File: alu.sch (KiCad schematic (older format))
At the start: 10 parts

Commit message: tiny fixes in annotation
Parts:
- U20: renamed from U?; footprint (none) -> Package_SO:TSSOP-14_4.4x5mm_P0.65mm; LCSC (none) -> C6807
- gave numbers to parts that had none: 3
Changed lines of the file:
@@
 AR Path="/5FEB4D4D/601578DD" Ref="U?"  Part="1"
 AR Path="/600A4AF3/600A5215/601578DD" Ref="U?"  Part="4"
-AR Path="/600A4AF3/601578DD" Ref="U?"  Part="1"
-F 0 "U?" H 8325 4975 50  0000 C CNN
+AR Path="/600A4AF3/601578DD" Ref="U21"  Part="1"
+F 0 "U21" H 8325 4975 50  0000 C CNN
 F 1 "74HC32" H 8325 4884 50  0000 C CNN
 F 2 "Housings_SOIC:SOIC-14_3.9x8.7mm_Pitch1.27mm" H 7800 4900 50  0001 C CNN
@@
 AR Path="/5FEB4D4D/60158F2A" Ref="U?"  Part="1"
 AR Path="/600A4AF3/600A5215/60158F2A" Ref="U?"  Part="4"
-AR Path="/600A4AF3/60158F2A" Ref="U?"  Part="3"
-F 0 "U?" H 8825 5225 50  0000 C CNN
+AR Path="/600A4AF3/60158F2A" Ref="U21"  Part="3"
+F 0 "U21" H 8825 5225 50  0000 C CNN
 F 1 "74HC32" H 8825 5134 50  0000 C CNN
 F 2 "Housings_SOIC:SOIC-14_3.9x8.7mm_Pitch1.27mm" H 8300 5150 50  0001 C CNN
@@
 AR Path="/5FEB4D4D/60159879" Ref="U?"  Part="1"
 AR Path="/600A4AF3/600A5215/60159879" Ref="U?"  Part="4"
-AR Path="/600A4AF3/60159879" Ref="U?"  Part="2"
-F 0 "U?" H 8325 5475 50  0000 C CNN
+AR Path="/600A4AF3/60159879" Ref="U21"  Part="2"
+F 0 "U21" H 8325 5475 50  0000 C CNN
 F 1 "74HC32" H 8325 5384 50  0000 C CNN
 F 2 "Housings_SOIC:SOIC-14_3.9x8.7mm_Pitch1.27mm" H 7800 5400 50  0001 C CNN
@@
 AR Path="/5FEB4D4D/601666B3" Ref="U?"  Part="1"
 AR Path="/600A4AF3/600A5215/601666B3" Ref="U?"  Part="4"
-AR Path="/600A4AF3/601666B3" Ref="U?"  Part="5"
-F 0 "U?" H 5725 7425 50  0000 C CNN
+AR Path="/600A4AF3/601666B3" Ref="U21"  Part="5"
+F 0 "U21" H 5725 7425 50  0000 C CNN
 F 1 "74HC32" H 5725 7334 50  0000 C CNN
 F 2 "Housings_SOIC:SOIC-14_3.9x8.7mm_Pitch1.27mm" H 5200 7350 50  0001 C CNN
@@
 P 9400 4950
 AR Path="/5FEB4D4D/601C1314" Ref="U?"  Part="4"
-AR Path="/600A4AF3/601C1314" Ref="U?"  Part="1"
-F 0 "U?" H 9400 5275 50  0000 C CNN
+AR Path="/600A4AF3/601C1314" Ref="U20"  Part="1"
+F 0 "U20" H 9400 5275 50  0000 C CNN
 F 1 "74HC00" H 9400 5184 50  0000 C CNN
 F 2 "Package_SO:TSSOP-14_4.4x5mm_P0.65mm" H 9400 4950 50  0001 C CNN
@@
 P 8750 3900
 AR Path="/5FEB4D4D/602410A7" Ref="U?"  Part="1"
-AR Path="/600A4AF3/602410A7" Ref="U?"  Part="1"
-F 0 "U?" H 8775 4167 50  0000 C CNN
+AR Path="/600A4AF3/602410A7" Ref="U22"  Part="1"
+F 0 "U22" H 8775 4167 50  0000 C CNN
 F 1 "74HC08" H 8775 4076 50  0000 C CNN
 F 2 "Housings_SOIC:SOIC-14_3.9x8.7mm_Pitch1.27mm" H 8750 3900 50  0001 C CNN
@@
 P 4900 7000
 AR Path="/5FEB4D4D/6029D5E1" Ref="U?"  Part="1"
-AR Path="/600A4AF3/6029D5E1" Ref="U?"  Part="5"
-F 0 "U?" H 4925 7267 50  0000 C CNN
+AR Path="/600A4AF3/6029D5E1" Ref="U22"  Part="5"
+F 0 "U22" H 4925 7267 50  0000 C CNN
 F 1 "74HC08" H 4925 7176 50  0000 C CNN
 F 2 "Housings_SOIC:SOIC-14_3.9x8.7mm_Pitch1.27mm" H 4900 7000 50  0001 C CNN
@@
 AR Path="/5FEB4D4D/602F6DA6" Ref="#PWR?"  Part="1"
 AR Path="/600A4AF3/600A5215/602F6DA6" Ref="#PWR?"  Part="1"
-AR Path="/600A4AF3/602F6DA6" Ref="#PWR?"  Part="1"
-F 0 "#PWR?" H 4900 6350 50  0001 C CNN
+AR Path="/600A4AF3/602F6DA6" Ref="#PWR0104"  Part="1"
+F 0 "#PWR0104" H 4900 6350 50  0001 C CNN
 F 1 "+5V" V 4915 6628 50  0000 L CNN
 F 2 "" H 4900 6500 50  0001 C CNN
@@
 AR Path="/5FEB4D4D/602F79FD" Ref="#PWR?"  Part="1"
 AR Path="/600A4AF3/600A5215/602F79FD" Ref="#PWR?"  Part="1"
-AR Path="/600A4AF3/602F79FD" Ref="#PWR?"  Part="1"
-F 0 "#PWR?" H 5450 6650 50  0001 C CNN
+AR Path="/600A4AF3/602F79FD" Ref="#PWR0105"  Part="1"
+F 0 "#PWR0105" H 5450 6650 50  0001 C CNN
 F 1 "+5V" V 5465 6928 50  0000 L CNN
 F 2 "" H 5450 6800 50  0001 C CNN
@@
 AR Path="/5FEB4D4D/602F80E1" Ref="#PWR?"  Part="1"
 AR Path="/600A4AF3/600A5215/602F80E1" Ref="#PWR?"  Part="1"
-AR Path="/600A4AF3/602F80E1" Ref="#PWR?"  Part="1"
-F 0 "#PWR?" H 6350 6150 50  0001 C CNN
+AR Path="/600A4AF3/602F80E1" Ref="#PWR0108"  Part="1"
+F 0 "#PWR0108" H 6350 6150 50  0001 C CNN
 F 1 "+5V" V 6365 6428 50  0000 L CNN
 F 2 "" H 6350 6300 50  0001 C CNN
@@
 AR Path="/5FEB4D4D/602F8A4B" Ref="#PWR?"  Part="1"
 AR Path="/600A4AF3/600A5215/602F8A4B" Ref="#PWR?"  Part="1"
-AR Path="/600A4AF3/602F8A4B" Ref="#PWR?"  Part="1"
-F 0 "#PWR?" H 4900 7250 50  0001 C CNN
+AR Path="/600A4AF3/602F8A4B" Ref="#PWR0109"  Part="1"
+F 0 "#PWR0109" H 4900 7250 50  0001 C CNN
 F 1 "GND" V 4905 7372 50  0000 R CNN
 F 2 "" H 4900 7500 50  0001 C CNN
@@
 AR Path="/5FEB4D4D/602F92D6" Ref="#PWR?"  Part="1"
 AR Path="/600A4AF3/600A5215/602F92D6" Ref="#PWR?"  Part="1"
-AR Path="/600A4AF3/602F92D6" Ref="#PWR?"  Part="1"
-F 0 "#PWR?" H 5450 7250 50  0001 C CNN
+AR Path="/600A4AF3/602F92D6" Ref="#PWR0110"  Part="1"
+F 0 "#PWR0110" H 5450 7250 50  0001 C CNN
 F 1 "GND" V 5455 7372 50  0000 R CNN
 F 2 "" H 5450 7500 50  0001 C CNN
@@
 AR Path="/5FEB4D4D/602F97D5" Ref="#PWR?"  Part="1"
 AR Path="/600A4AF3/600A5215/602F97D5" Ref="#PWR?"  Part="1"
-AR Path="/600A4AF3/602F97D5" Ref="#PWR?"  Part="1"
-F 0 "#PWR?" H 6350 7050 50  0001 C CNN
+AR Path="/600A4AF3/602F97D5" Ref="#PWR0111"  Part="1"
+F 0 "#PWR0111" H 6350 7050 50  0001 C CNN
 F 1 "GND" V 6355 7172 50  0000 R CNN
 F 2 "" H 6350 7300 50  0001 C CNN
@@
 P 6350 6800
 AR Path="/5FEB4D4D/601C131B" Ref="U?"  Part="5"
-AR Path="/600A4AF3/601C131B" Ref="U?"  Part="5"
-F 0 "U?" H 6580 6846 50  0000 L CNN
+AR Path="/600A4AF3/601C131B" Ref="U20"  Part="5"
+F 0 "U20" H 6580 6846 50  0000 L CNN
 F 1 "74HC00" H 6580 6755 50  0000 L CNN
 F 2 "Package_SO:TSSOP-14_4.4x5mm_P0.65mm" H 6350 6800 50  0001 C CNN
@@
 P 6050 5350
 AR Path="/5FEB4D4D/601C1306" Ref="U?"  Part="2"
-AR Path="/600A4AF3/601C1306" Ref="U?"  Part="2"
-F 0 "U?" H 6050 5675 50  0000 C CNN
+AR Path="/600A4AF3/601C1306" Ref="U20"  Part="2"
+F 0 "U20" H 6050 5675 50  0000 C CNN
 F 1 "74HC00" H 6050 5584 50  0000 C CNN
 F 2 "Package_SO:TSSOP-14_4.4x5mm_P0.65mm" H 6050 5350 50  0001 C CNN
@@
 	2650 4650 2650 5050
 $Comp
-L 74xx:74HC00 U?
+L 74xx:74HC00 U20
 U 3 1 603629D0
 P 2650 5350
-F 0 "U?" V 2696 5170 50  0000 R CNN
+F 0 "U20" V 2696 5170 50  0000 R CNN
 F 1 "74HC00" V 2605 5170 50  0000 R CNN
-F 2 "" H 2650 5350 50  0001 C CNN
-F 3 "http://www.ti.com/lit/gpn/sn74hc00" H 2650 5350 50  0001 C CNN
+F 2 "Package_SO:TSSOP-14_4.4x5mm_P0.65mm" H 2650 5350 50  0001 C CNN
+F 3 "https://datasheet.lcsc.com/szlcsc/Texas-Instruments-TI-SN74HC00PWR_C6807.pdf" H 2650 5350 50  0001 C CNN
+F 4 "C6807" V 2650 5350 50  0001 C CNN "LCSC"
 	3    2650 5350
 	0    -1   -1   0

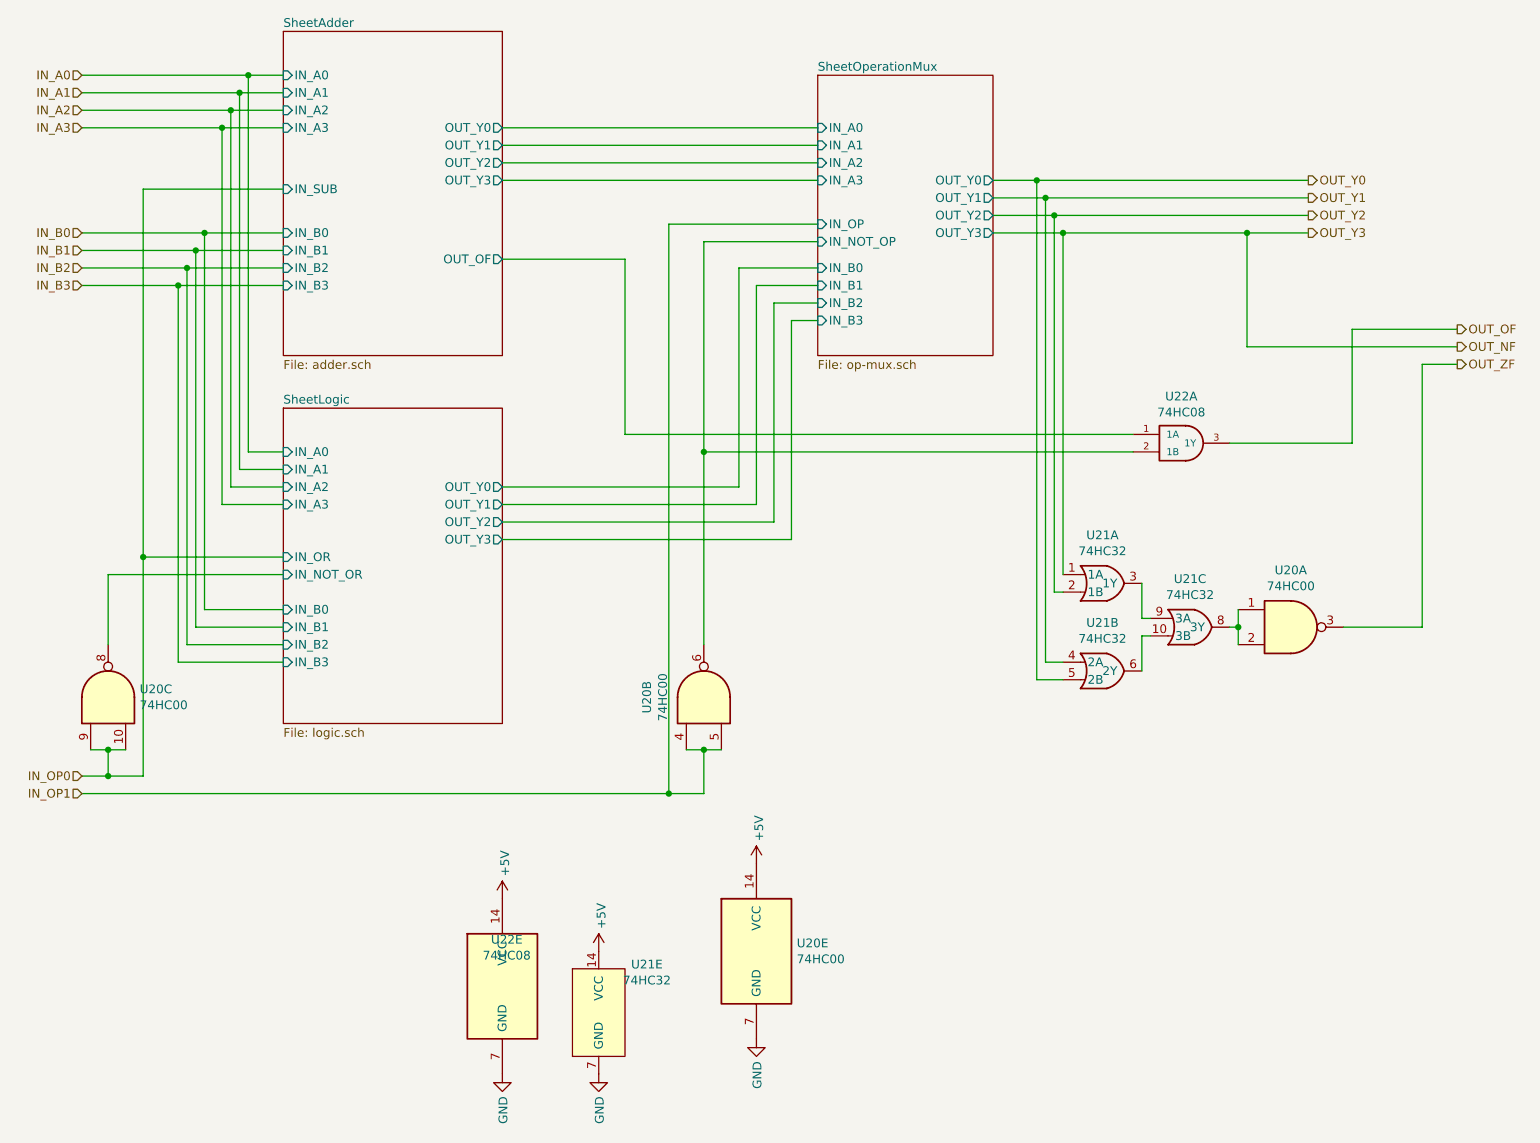
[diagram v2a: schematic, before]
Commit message: exchanged a single AND
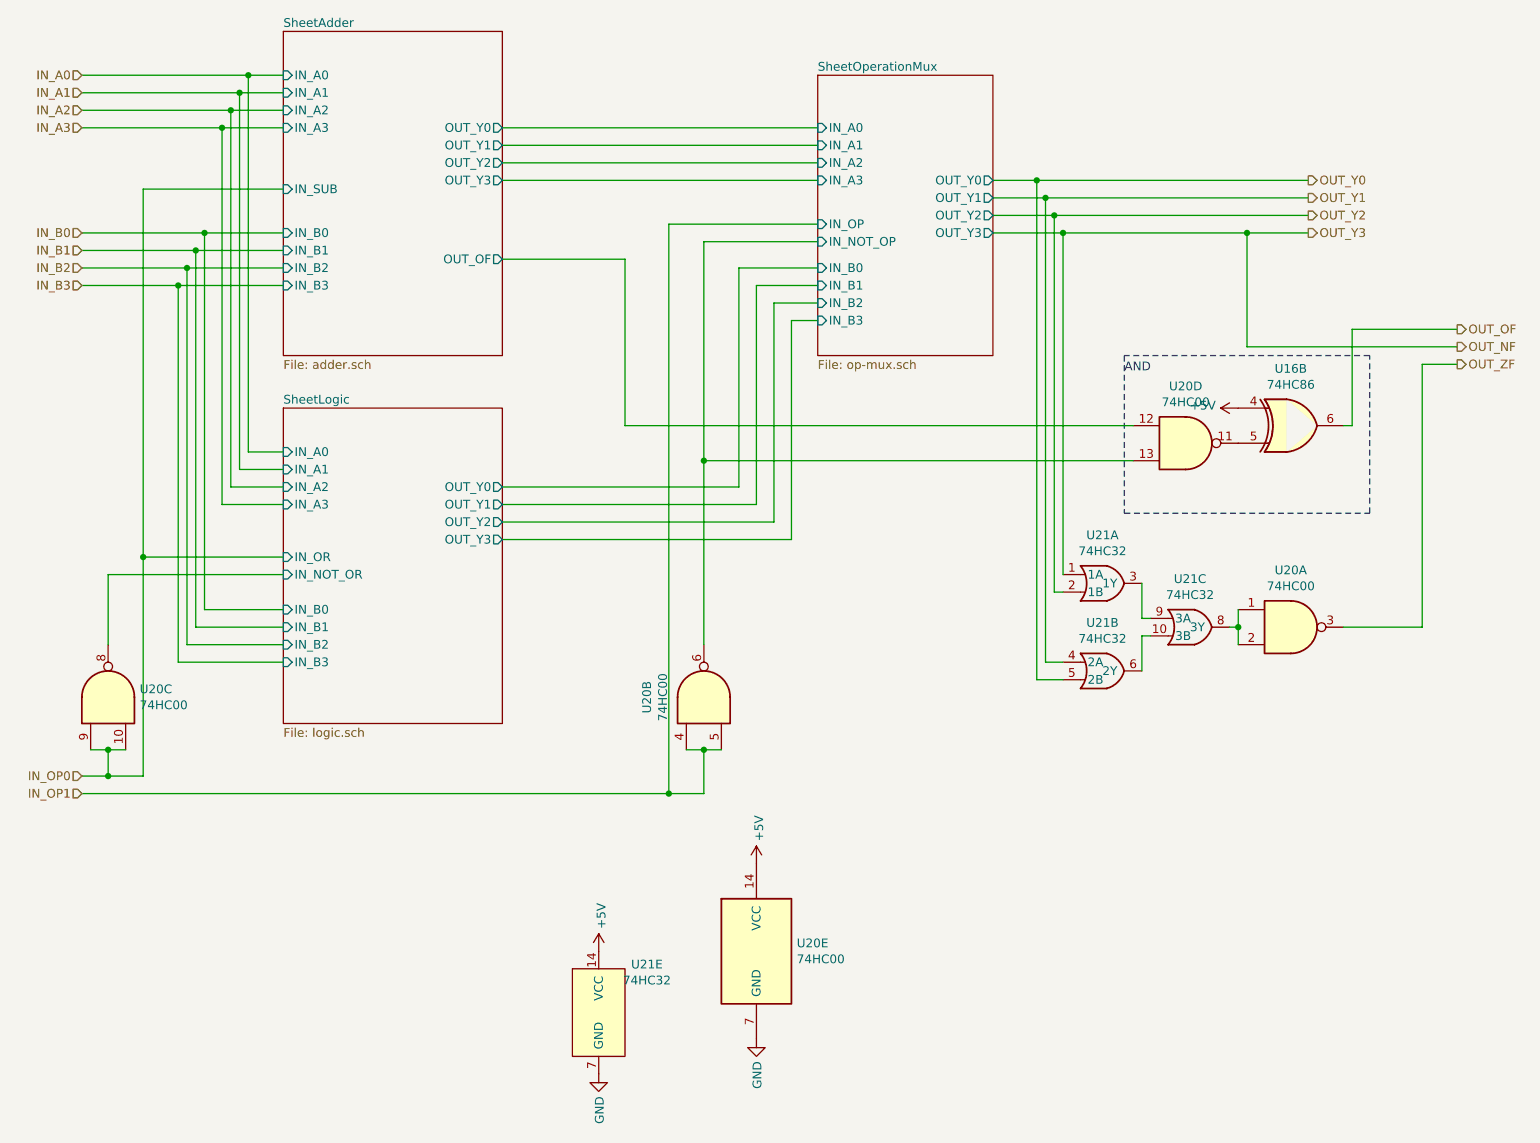
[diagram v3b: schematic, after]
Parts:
- removed U22: 74HC08, Housings_SOIC:SOIC-14_3.9x8.7mm_Pitch1.27mm, symbol PB170:74HC08
- added U16: 74HC86, symbol 74xx:74HC86
- added unit 4 of U20
- U20: footprint Package_SO:TSSOP-14_4.4x5mm_P0.65mm -> (none)
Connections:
- net +5V: now also U16.4
- net OUT_OF: now also U16.6
- net SheetAdder/OUT_OF: now also U20.12
- net SheetOperationMux/IN_NOT_OP: now also U20.13
- new net: U16.5, U20.11
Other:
- note added: "AND"
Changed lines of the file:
@@
 F 0 "U20" H 9400 5275 50  0000 C CNN
 F 1 "74HC00" H 9400 5184 50  0000 C CNN
-F 2 "Package_SO:TSSOP-14_4.4x5mm_P0.65mm" H 9400 4950 50  0001 C CNN
-F 3 "https://datasheet.lcsc.com/szlcsc/Texas-Instruments-TI-SN74HC00PWR_C6807.pdf" H 9400 4950 50  0001 C CNN
+F 2 "" H 9400 4950 50  0001 C CNN
+F 3 "http://www.ti.com/lit/gpn/sn74hc00" H 9400 4950 50  0001 C CNN
 F 4 "C6807" H 9400 4950 50  0001 C CNN "LCSC"
 	1    9400 4950
@@
 Wire Wire Line
 	4900 2850 5600 2850
-$Comp
-L PB170:74HC08 U?
-U 1 1 602410A7
-P 8750 3900
-AR Path="/5FEB4D4D/602410A7" Ref="U?"  Part="1"
-AR Path="/600A4AF3/602410A7" Ref="U22"  Part="1"
-F 0 "U22" H 8775 4167 50  0000 C CNN
-F 1 "74HC08" H 8775 4076 50  0000 C CNN
-F 2 "Housings_SOIC:SOIC-14_3.9x8.7mm_Pitch1.27mm" H 8750 3900 50  0001 C CNN
-F 3 "https://datasheet.lcsc.com/szlcsc/Nexperia-74HC08D-653_C5593.pdf" H 8750 3900 50  0001 C CNN
-F 4 "C5593" H 8750 3900 50  0001 C CNN "LCSC"
-	1    8750 3900
-	1    0    0    -1
-$EndComp
 Wire Wire Line
 	10350 3250 9750 3250
-Wire Wire Line
-	9750 3250 9750 3900
-Wire Wire Line
-	9750 3900 9050 3900
 Wire Wire Line
 	8100 4650 8100 2700
@@
 Wire Wire Line
 	7950 2400 9500 2400
-$Comp
-L PB170:74HC08 U?
-U 5 1 6029D5E1
-P 4900 7000
-AR Path="/5FEB4D4D/6029D5E1" Ref="U?"  Part="1"
-AR Path="/600A4AF3/6029D5E1" Ref="U22"  Part="5"
-F 0 "U22" H 4925 7267 50  0000 C CNN
-F 1 "74HC08" H 4925 7176 50  0000 C CNN
-F 2 "Housings_SOIC:SOIC-14_3.9x8.7mm_Pitch1.27mm" H 4900 7000 50  0001 C CNN
-F 3 "https://datasheet.lcsc.com/szlcsc/Nexperia-74HC08D-653_C5593.pdf" H 4900 7000 50  0001 C CNN
-F 4 "C5593" H 4900 7000 50  0001 C CNN "LCSC"
-	5    4900 7000
-	1    0    0    -1
-$EndComp
 Connection ~ 2850 4550
 Text HLabel 2500 5800 0    50   Input ~ 0
@@
 Wire Wire Line
 	2850 5800 2850 4550
-$Comp
-L power:+5V #PWR?
-U 1 1 602F6DA6
-P 4900 6500
-AR Path="/602F6DA6" Ref="#PWR?"  Part="1"
-AR Path="/5FEB4D4D/602F6DA6" Ref="#PWR?"  Part="1"
-AR Path="/600A4AF3/600A5215/602F6DA6" Ref="#PWR?"  Part="1"
-AR Path="/600A4AF3/602F6DA6" Ref="#PWR0104"  Part="1"
-F 0 "#PWR0104" H 4900 6350 50  0001 C CNN
-F 1 "+5V" V 4915 6628 50  0000 L CNN
-F 2 "" H 4900 6500 50  0001 C CNN
-F 3 "" H 4900 6500 50  0001 C CNN
-	1    4900 6500
-	1    0    0    -1
-$EndComp
 $Comp
 L power:+5V #PWR?
@@
 F 3 "" H 6350 6300 50  0001 C CNN
 	1    6350 6300
-	1    0    0    -1
-$EndComp
-$Comp
-L power:GND #PWR?
-U 1 1 602F8A4B
-P 4900 7500
-AR Path="/602F8A4B" Ref="#PWR?"  Part="1"
-AR Path="/5FEB4D4D/602F8A4B" Ref="#PWR?"  Part="1"
-AR Path="/600A4AF3/600A5215/602F8A4B" Ref="#PWR?"  Part="1"
-AR Path="/600A4AF3/602F8A4B" Ref="#PWR0109"  Part="1"
-F 0 "#PWR0109" H 4900 7250 50  0001 C CNN
-F 1 "GND" V 4905 7372 50  0000 R CNN
-F 2 "" H 4900 7500 50  0001 C CNN
-F 3 "" H 4900 7500 50  0001 C CNN
-	1    4900 7500
 	1    0    0    -1
 $EndComp
@@
 F 0 "U20" H 6580 6846 50  0000 L CNN
 F 1 "74HC00" H 6580 6755 50  0000 L CNN
-F 2 "Package_SO:TSSOP-14_4.4x5mm_P0.65mm" H 6350 6800 50  0001 C CNN
-F 3 "https://datasheet.lcsc.com/szlcsc/Texas-Instruments-TI-SN74HC00PWR_C6807.pdf" H 6350 6800 50  0001 C CNN
+F 2 "" H 6350 6800 50  0001 C CNN
+F 3 "http://www.ti.com/lit/gpn/sn74hc00" H 6350 6800 50  0001 C CNN
 F 4 "C6807" H 6350 6800 50  0001 C CNN "LCSC"
 	5    6350 6800
@@
 F 0 "U20" H 6050 5675 50  0000 C CNN
 F 1 "74HC00" H 6050 5584 50  0000 C CNN
-F 2 "Package_SO:TSSOP-14_4.4x5mm_P0.65mm" H 6050 5350 50  0001 C CNN
-F 3 "https://datasheet.lcsc.com/szlcsc/Texas-Instruments-TI-SN74HC00PWR_C6807.pdf" H 6050 5350 50  0001 C CNN
+F 2 "" H 6050 5350 50  0001 C CNN
+F 3 "http://www.ti.com/lit/gpn/sn74hc00" H 6050 5350 50  0001 C CNN
 F 4 "C6807" H 6050 5350 50  0001 C CNN "LCSC"
 	2    6050 5350
@@
 Wire Wire Line
 	6050 2750 6700 2750
-Wire Wire Line
-	5600 2850 5600 3850
-Wire Wire Line
-	5600 3850 8500 3850
-Wire Wire Line
-	8500 3950 6050 3950
-Wire Wire Line
-	6050 2750 6050 3950
-Connection ~ 6050 3950
-Wire Wire Line
-	6050 3950 6050 5050
 Wire Wire Line
 	2650 4650 2650 5050
@@
 F 0 "U20" V 2696 5170 50  0000 R CNN
 F 1 "74HC00" V 2605 5170 50  0000 R CNN
-F 2 "Package_SO:TSSOP-14_4.4x5mm_P0.65mm" H 2650 5350 50  0001 C CNN
-F 3 "https://datasheet.lcsc.com/szlcsc/Texas-Instruments-TI-SN74HC00PWR_C6807.pdf" H 2650 5350 50  0001 C CNN
+F 2 "" H 2650 5350 50  0001 C CNN
+F 3 "http://www.ti.com/lit/gpn/sn74hc00" H 2650 5350 50  0001 C CNN
 F 4 "C6807" V 2650 5350 50  0001 C CNN "LCSC"
 	3    2650 5350
 	0    -1   -1   0
 $EndComp
+$Comp
+L 74xx:74HC00 U20
+U 4 1 60249F57
+P 8800 3900
+F 0 "U20" H 8800 4225 50  0000 C CNN
+F 1 "74HC00" H 8800 4134 50  0000 C CNN
+F 2 "" H 8800 3900 50  0001 C CNN
+F 3 "http://www.ti.com/lit/gpn/sn74hc00" H 8800 3900 50  0001 C CNN
+	4    8800 3900
+	1    0    0    -1
+$EndComp
+$Comp
+L 74xx:74HC86 U16
+U 2 1 6026643A
+P 9400 3800
+F 0 "U16" H 9400 4125 50  0000 C CNN
+F 1 "74HC86" H 9400 4034 50  0000 C CNN
+F 2 "" H 9400 3800 50  0001 C CNN
+F 3 "http://www.ti.com/lit/gpn/sn74HC86" H 9400 3800 50  0001 C CNN
+	2    9400 3800
+	1    0    0    -1
+$EndComp
+$Comp
+L power:+5V #PWR?
+U 1 1 602768A6
+P 9100 3700
+AR Path="/602768A6" Ref="#PWR?"  Part="1"
+AR Path="/5FEB4D4D/602768A6" Ref="#PWR?"  Part="1"
+AR Path="/600A4AF3/600A5215/602768A6" Ref="#PWR?"  Part="1"
+AR Path="/600A4AF3/602768A6" Ref="#PWR?"  Part="1"
+F 0 "#PWR?" H 9100 3550 50  0001 C CNN
+F 1 "+5V" V 9115 3828 50  0000 L CNN
+F 2 "" H 9100 3700 50  0001 C CNN
+F 3 "" H 9100 3700 50  0001 C CNN
+	1    9100 3700
+	0    -1   -1   0
+$EndComp
+Wire Wire Line
+	5600 2850 5600 3800
+Wire Wire Line
+	8500 4000 6050 4000
+Connection ~ 6050 4000
+Wire Wire Line
+	6050 4000 6050 5050
+Wire Wire Line
+	6050 2750 6050 4000
+Wire Wire Line
+	8500 3800 5600 3800
+Wire Wire Line
+	9700 3800 9750 3800
+Wire Wire Line
+	9750 3800 9750 3250
+Wire Notes Line
+	8450 4300 9850 4300
+Wire Notes Line
+	9850 4300 9850 3400
+Wire Notes Line
+	9850 3400 8450 3400
+Wire Notes Line
+	8450 3400 8450 4300
+Text Notes 8450 3500 0    50   ~ 0
+AND
 $EndSCHEMATC

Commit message: minor fixes
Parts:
- added unit 3 of U16
- added unit 4 of U16
- added unit 4 of U21
- U16: footprint (none) -> Package_SO:TSSOP-14_4.4x5mm_P0.65mm
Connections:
- no-connect marks 0 -> 9
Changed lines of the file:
@@
 $Descr A4 11693 8268
 encoding utf-8
-Sheet 3 9
+Sheet 2 8
 Title ""
 Date ""
@@
 F 0 "U16" H 9400 4125 50  0000 C CNN
 F 1 "74HC86" H 9400 4034 50  0000 C CNN
-F 2 "" H 9400 3800 50  0001 C CNN
-F 3 "http://www.ti.com/lit/gpn/sn74HC86" H 9400 3800 50  0001 C CNN
+F 2 "Package_SO:TSSOP-14_4.4x5mm_P0.65mm" H 9400 3800 50  0001 C CNN
+F 3 "https://datasheet.lcsc.com/szlcsc/Texas-Instruments-TI-SN74AHC86PWR_C117522.pdf" H 9400 3800 50  0001 C CNN
 	2    9400 3800
 	1    0    0    -1
@@
 Text Notes 8450 3500 0    50   ~ 0
 AND
+$Comp
+L PB170:74HC32 U?
+U 4 1 602AE295
+P 8350 5850
+AR Path="/5FEB4D4D/602AE295" Ref="U?"  Part="1"
+AR Path="/600A4AF3/600A5215/602AE295" Ref="U?"  Part="4"
+AR Path="/600A4AF3/602AE295" Ref="U21"  Part="4"
+F 0 "U21" H 8325 6125 50  0000 C CNN
+F 1 "74HC32" H 8325 6034 50  0000 C CNN
+F 2 "Housings_SOIC:SOIC-14_3.9x8.7mm_Pitch1.27mm" H 7800 6050 50  0001 C CNN
+F 3 "https://datasheet.lcsc.com/szlcsc/Nexperia-74HC32D-653_C5632.pdf" H 7800 6050 50  0001 C CNN
+F 4 "C5632" H 8350 5850 50  0001 C CNN "LCSC"
+	4    8350 5850
+	1    0    0    -1
+$EndComp
+NoConn ~ 8100 5800
+NoConn ~ 8100 5900
+NoConn ~ 8550 5850
+$Comp
+L 74xx:74HC86 U?
+U 3 1 60302642
+P 7100 5450
+AR Path="/5FEB4D4D/60302642" Ref="U?"  Part="2"
+AR Path="/600A4AF3/600A5215/60302642" Ref="U?"  Part="1"
+AR Path="/600A4AF3/60302642" Ref="U16"  Part="3"
+F 0 "U16" H 7100 5775 50  0000 C CNN
+F 1 "74HC86" H 7100 5684 50  0000 C CNN
+F 2 "Package_SO:TSSOP-14_4.4x5mm_P0.65mm" H 7100 5450 50  0001 C CNN
+F 3 "https://datasheet.lcsc.com/szlcsc/Texas-Instruments-TI-SN74AHC86PWR_C117522.pdf" H 7100 5450 50  0001 C CNN
+F 4 "C117522" H 7100 5450 50  0001 C CNN "LCSC"
+	3    7100 5450
+	1    0    0    -1
+$EndComp
+NoConn ~ 7400 5450
+NoConn ~ 6800 5550
+NoConn ~ 6800 5350
+$Comp
+L 74xx:74HC86 U?
+U 4 1 6032D615
+P 9350 5800
+AR Path="/5FEB4D4D/6032D615" Ref="U?"  Part="2"
+AR Path="/600A4AF3/600A5215/6032D615" Ref="U?"  Part="1"
+AR Path="/600A4AF3/6032D615" Ref="U16"  Part="4"
+F 0 "U16" H 9350 6125 50  0000 C CNN
+F 1 "74HC86" H 9350 6034 50  0000 C CNN
+F 2 "Package_SO:TSSOP-14_4.4x5mm_P0.65mm" H 9350 5800 50  0001 C CNN
+F 3 "https://datasheet.lcsc.com/szlcsc/Texas-Instruments-TI-SN74AHC86PWR_C117522.pdf" H 9350 5800 50  0001 C CNN
+F 4 "C117522" H 9350 5800 50  0001 C CNN "LCSC"
+	4    9350 5800
+	1    0    0    -1
+$EndComp
+NoConn ~ 9650 5800
+NoConn ~ 9050 5900
+NoConn ~ 9050 5700
 $EndSCHEMATC
